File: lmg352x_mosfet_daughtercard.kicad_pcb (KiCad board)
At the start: 2 copper layers, 67 parts

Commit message: Changes(02092025)
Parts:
- D5: moved to B.Cu
- D7: moved to F.Cu
- moved C6 78.1 mm to (122.8, 71.5), turned to -90 degrees
- moved C5 70.9 mm to (115.8, 71.5), turned to -90 degrees
- moved U6 65.9 mm to (98.6, 82.6), turned to 180 degrees
- moved C11 65.0 mm to (145.5, 44.8)
- moved D7 59.6 mm to (136.2, 45.8), turned to 180 degrees
- moved U4 58.8 mm to (110.5, 72.0), turned to 180 degrees
- moved U8 58.7 mm to (159.8, 97.3)
- moved U7 58.0 mm to (143.8, 97.0)
- moved D5 55.4 mm to (84.8, 70.5), turned to 90 degrees
- moved L2 50.1 mm to (119.3, 71.6)
- moved TR2 45.0 mm to (98.8, 71.5)
- moved U3 45.0 mm to (89.0, 71.5)
- moved C4 39.8 mm to (84.8, 70.5), turned to 90 degrees
- moved C9 36.9 mm to (125.2, 42.7)
- moved C10 36.9 mm to (125.2, 45.7)
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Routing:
- net +5V: track 8.02 -> 14.1 mm
- net Net-(U4--): track 0.00 -> 5.83 mm
- net Net-(U4-+): track 0.00 -> 5.75 mm
- net Net-(U3-D1): track 0.00 -> 3.63 mm
- net Net-(U3-D2): track 0.00 -> 3.62 mm
- net Net-(U4-~_2): track 0.00 -> 3.19 mm
- net Net-(U4-~_1): track 0.00 -> 3.17 mm
- net +ISO_12V_H: track 0.00 -> 2.84 mm
- net Net-(U2--): track 2.87 -> 5.72 mm
- net SW: track 0.00 -> 2.83 mm
- net Net-(U2-+): track 2.87 -> 5.71 mm
- net +ISO_12V_L: track 0.00 -> 2.81 mm
- net GNDPWR: track 0.00 -> 2.72 mm
- net Net-(U1-D2): track 4.19 -> 3.62 mm

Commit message: Changes(02092025)
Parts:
- C10, C11, C12, C13, C14, C15, C16, C17, C18, C24, C25, C7, C8, C9, U7, U8: moved to B.Cu
- moved R8 133.4 mm to (159.9, 105.8), turned to -90 degrees
- moved C19 122.1 mm to (160.3, 113.4), turned to 90 degrees
- moved D1 119.8 mm to (155.3, 108.2), turned to 180 degrees
- moved C18 119.5 mm to (159.9, 105.8), turned to 90 degrees
- moved R10 118.9 mm to (145.8, 106.8)
- moved C30 118.8 mm to (169.6, 105.3)
- moved C31 118.8 mm to (169.6, 108.6)
- moved C27 117.9 mm to (169.4, 112.3)
- moved C28 117.9 mm to (169.4, 116.5)
- moved C29 117.9 mm to (169.4, 120.8)
- moved C32 113.5 mm to (169.6, 102.2)
- moved C21 111.0 mm to (154.9, 105.9), turned to 180 degrees
- moved D2 106.2 mm to (140.7, 108.2), turned to 180 degrees
- moved R11 105.1 mm to (125.2, 117.0), turned to 90 degrees
- moved R12 104.1 mm to (127.9, 114.1), turned to 90 degrees
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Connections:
- C10 pad 2: HS_PWM -> Net-(U5-IND)
- C12 pad 2: HS_PWM -> Net-(U6-IND)
- R3 pad 1: HS_CO/ZVD -> HS_OC/ZVD
- R4 pad 1: HS_PWM -> LS_PWM
- R5 pad 1: HS_FAULT -> LS_FAULT
- R6 pad 1: HS_CO/ZVD -> LS_OC/ZVD
- U6 pad 14: HS_TEMP -> LS_TEMP
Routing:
- net +5V_ISO_H: track 0.00 -> 81.0 mm, vias 0 -> 1
- net +5V_ISO_L: track 0.00 -> 67.5 mm, vias 0 -> 1
- net Net-(U5-INB): track 0.16 -> 64.9 mm, vias 0 -> 2
- net Net-(U5-INC): track 0.00 -> 64.7 mm, vias 0 -> 2
- net Net-(U5-INA): track 0.00 -> 63.8 mm, vias 0 -> 2
- net Net-(U5-OUTD): track 0.00 -> 58.3 mm, vias 0 -> 2
- net Net-(U6-INA): track 0.00 -> 54.0 mm, vias 0 -> 2
- net Net-(U6-INB): track 0.00 -> 52.4 mm, vias 0 -> 2
- net Net-(U6-INC): track 0.00 -> 50.7 mm, vias 0 -> 2
- net Net-(U6-OUTD): track 0.00 -> 47.7 mm, vias 0 -> 2
- net Net-(U7A-RDRV): track 0.00 -> 47.5 mm, vias 0 -> 2
- net +ISO_12V_H: track 2.84 -> 48.7 mm, vias 0 -> 1
- net +5V: track 14.1 -> 59.2 mm
- net Net-(U8A-RDRV): track 0.00 -> 31.4 mm, vias 0 -> 2
- net +ISO_12V_L: track 2.81 -> 31.4 mm, vias 0 -> 1
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- added copper zone on B.Cu, net GNDPWR
- added copper zone on F.Cu, net GNDPWR
- added copper zone on In1.Cu, net GNDPWR
- added copper zone on In2.Cu, net GNDPWR
- added copper zone on B.Cu, net HVBUS
- added copper zone on F.Cu, net HVBUS
- added copper zone on B.Cu, net SW
- added copper zone on F.Cu, net SW
- added copper zone on In1.Cu, net SW
- added copper zone on In2.Cu, net SW
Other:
- copper layers 2 -> 4

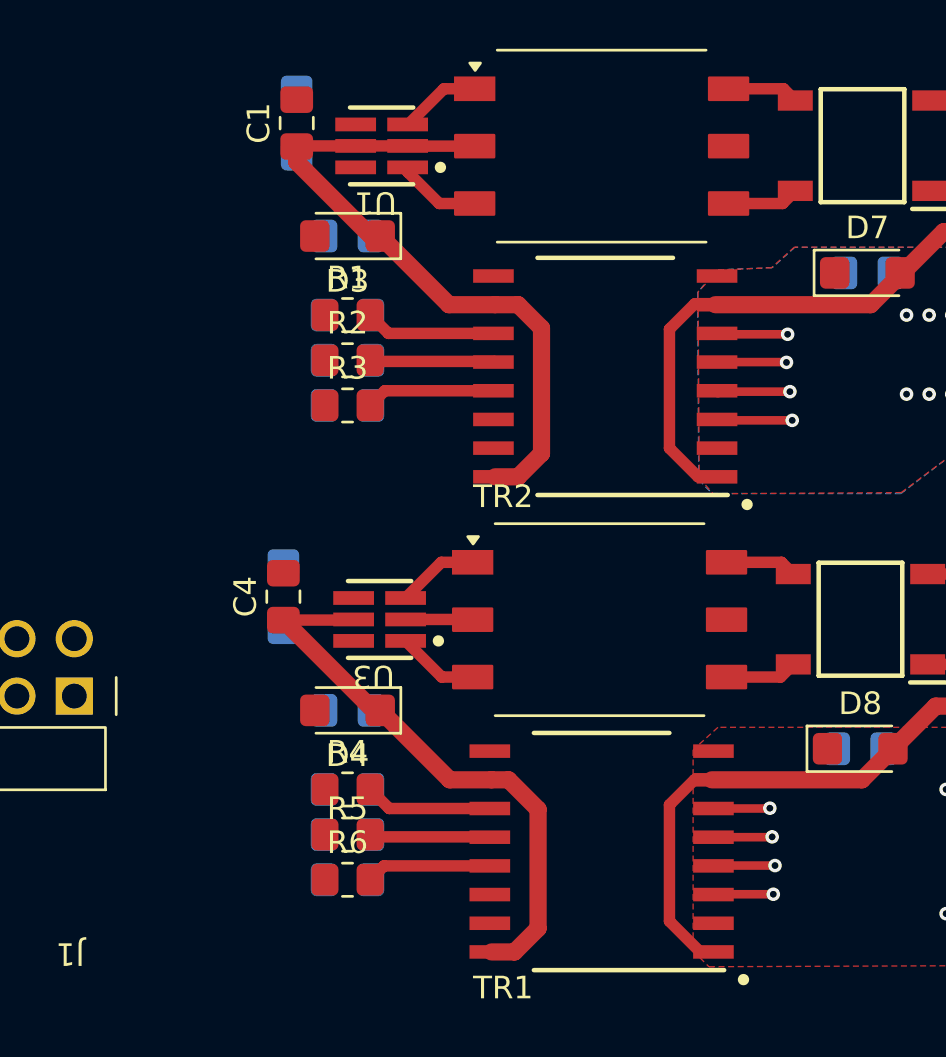
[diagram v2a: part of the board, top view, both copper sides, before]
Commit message: added vias
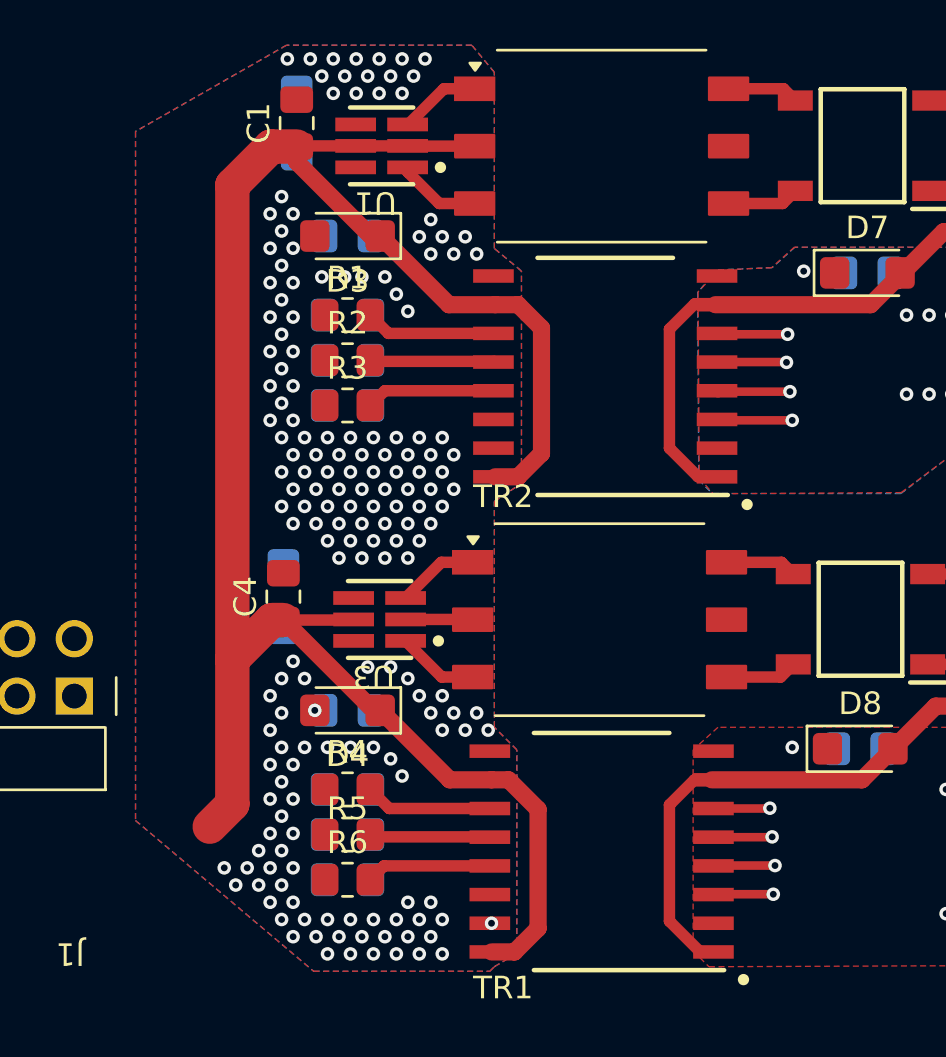
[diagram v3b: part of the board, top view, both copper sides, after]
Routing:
- net +5V: track 59.2 -> 94.6 mm
- net SW: vias 185 -> 186
- net GNDPWR: vias 123 -> 124
- net GNDA: vias 0 -> 174
- added copper zone on B.Cu, net GNDA
- added copper zone on F.Cu, net GNDA
- added copper zone on In1.Cu, net GNDA
- added copper zone on In2.Cu, net GNDA

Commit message: added via for PGND
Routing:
- net GNDPWR: vias 124 -> 125
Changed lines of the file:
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@@
+	)
+	(via
+		(at 123.5 116.5)
+		(size 0.6)
+		(drill 0.3)
+		(layers "F.Cu" "B.Cu")
+		(free yes)
+		(net 9)
 	)
 	(via

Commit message: little changes in 15.9.2025
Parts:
- removed J1: ~, KiCAD_Library-N1-V1.0:PinHeader_2x6_Angled
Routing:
- net GNDPWR: track 2.72 -> 11.1 mm
- net +5V: track 94.6 -> 86.8 mm
- net Net-(C26-Pad2): track 0.65 -> 4.34 mm, vias 0 -> 1
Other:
- board outline added: 97.5 x 45 mm
